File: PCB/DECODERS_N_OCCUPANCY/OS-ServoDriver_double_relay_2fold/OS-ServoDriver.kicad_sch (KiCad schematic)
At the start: 9 parts, among them J101 POWER, J102 DCC_FROG, J103 DCC_SIGNAL, SW101 SW_Push, SW102 SW_Push, SW103 SW_Push, SW104 SW_Push

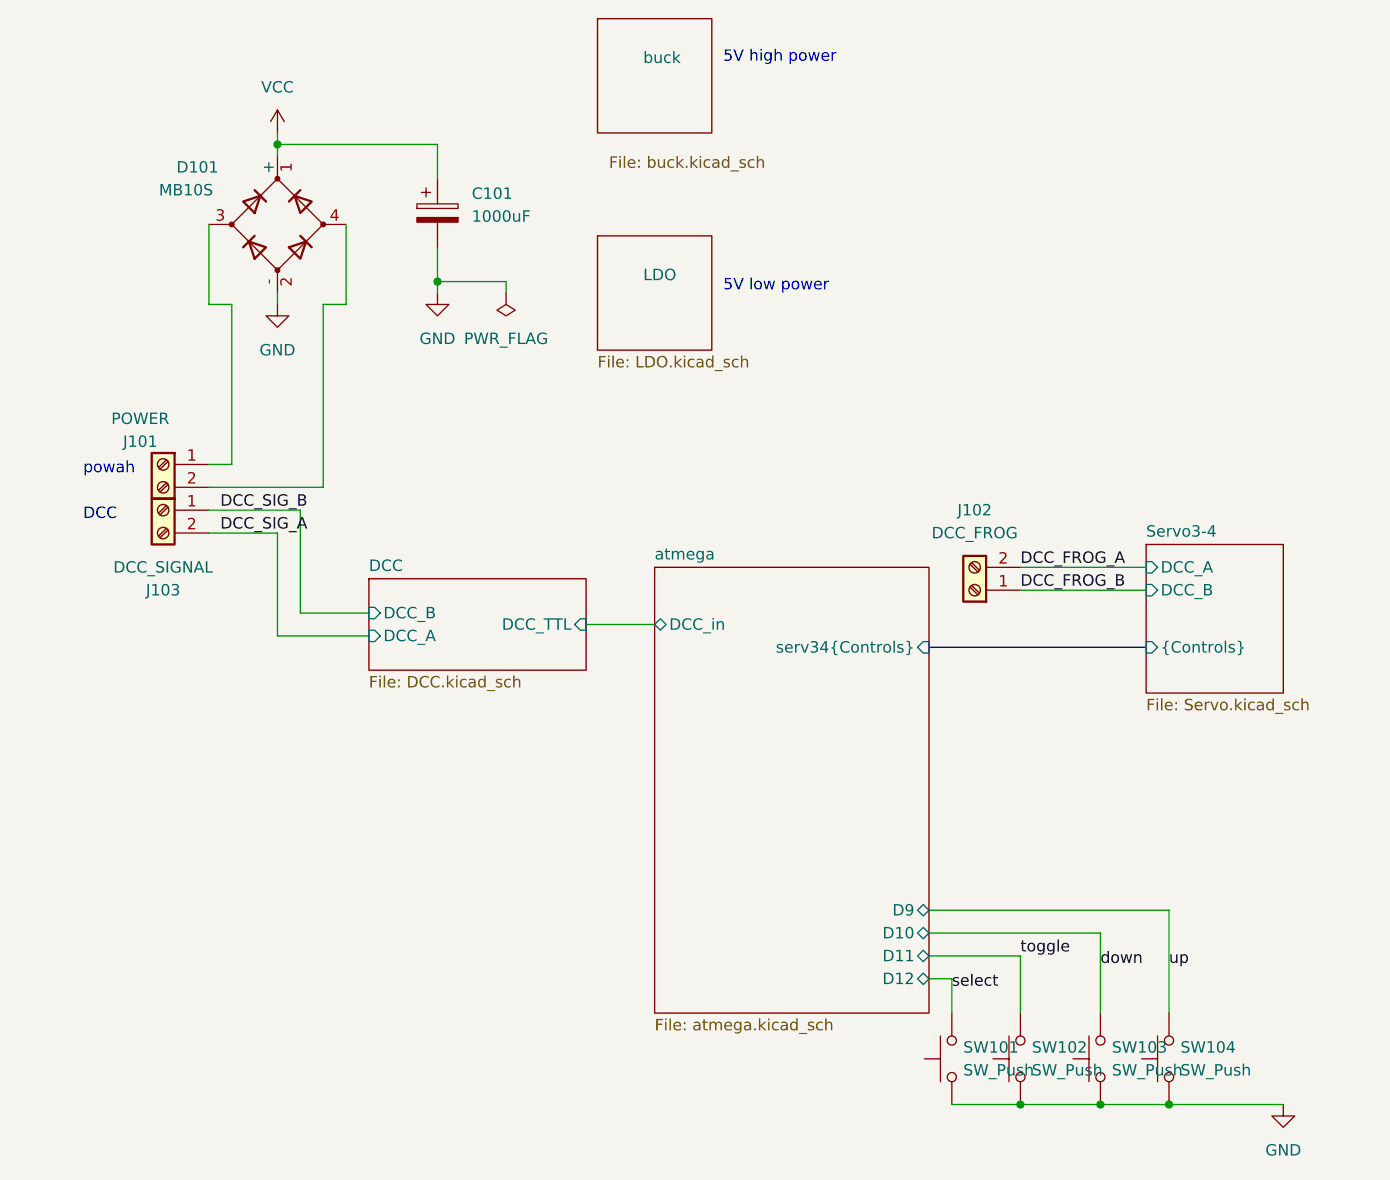
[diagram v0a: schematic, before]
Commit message: added some board files and Xnet block unit binary
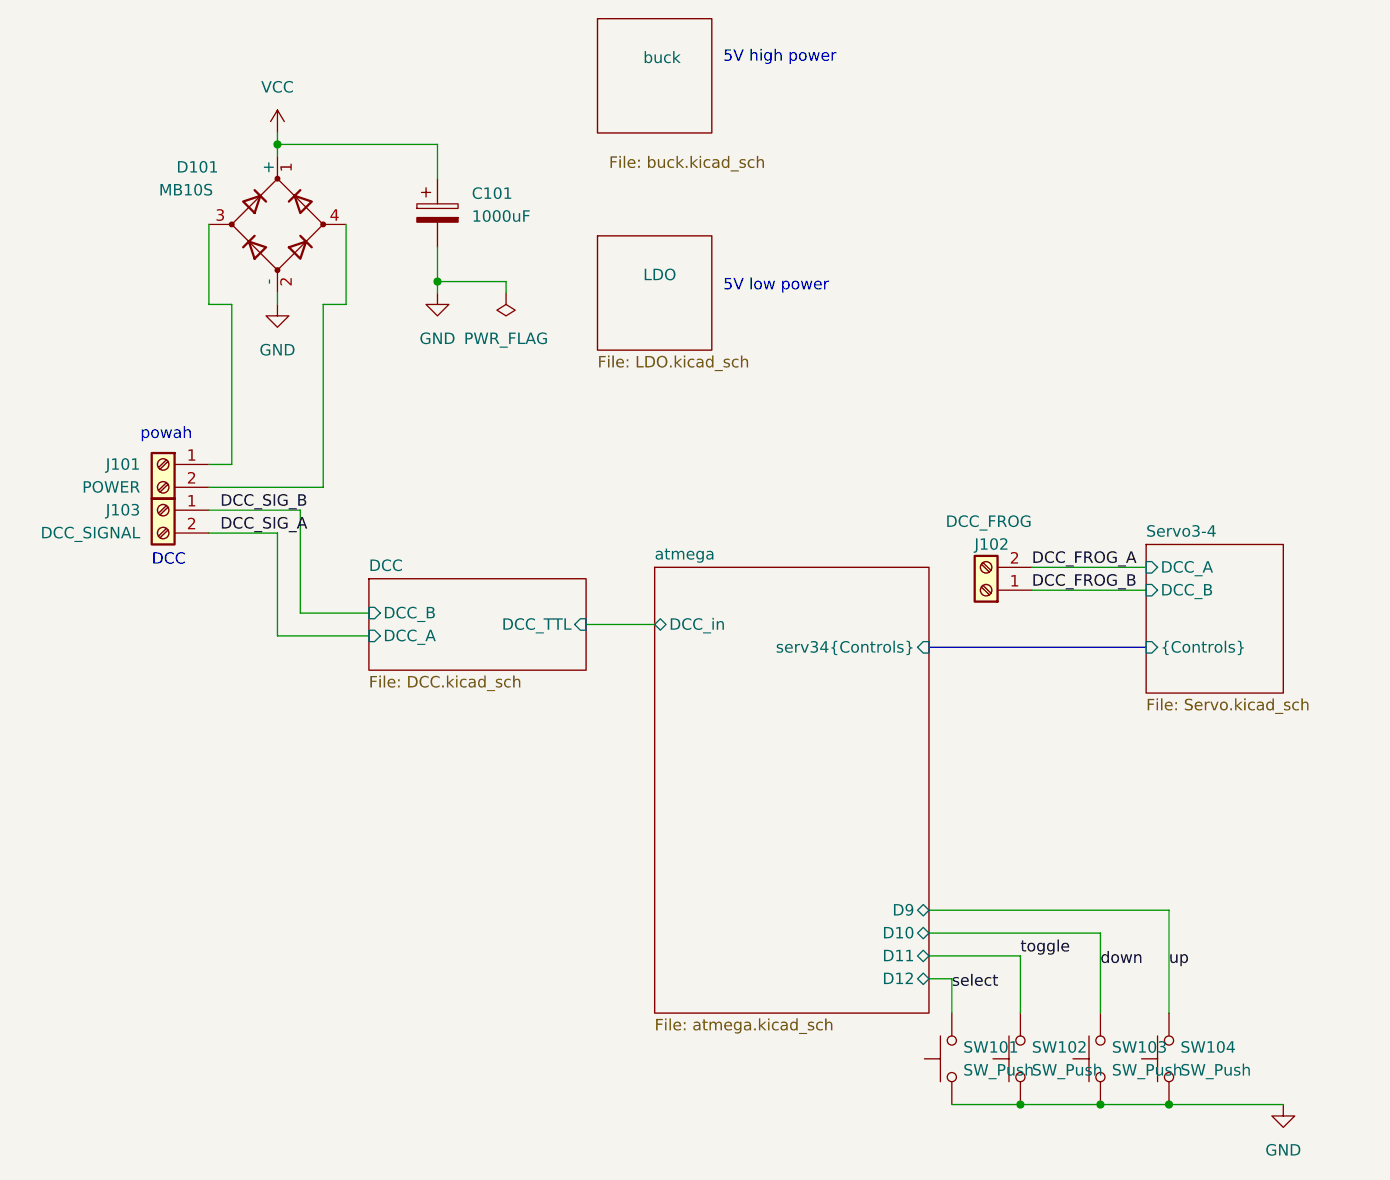
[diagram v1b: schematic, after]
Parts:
- J101, J102, J103: JLCPCB Part# (none) -> C8465
